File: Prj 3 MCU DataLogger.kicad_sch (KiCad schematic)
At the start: 25 parts, among them U1 24LC1025, U2 24LC1025, U3 DS1337S_, U4 ATMEGA328P-AU, Y1 16 MHz, Y2 32.768 KHz

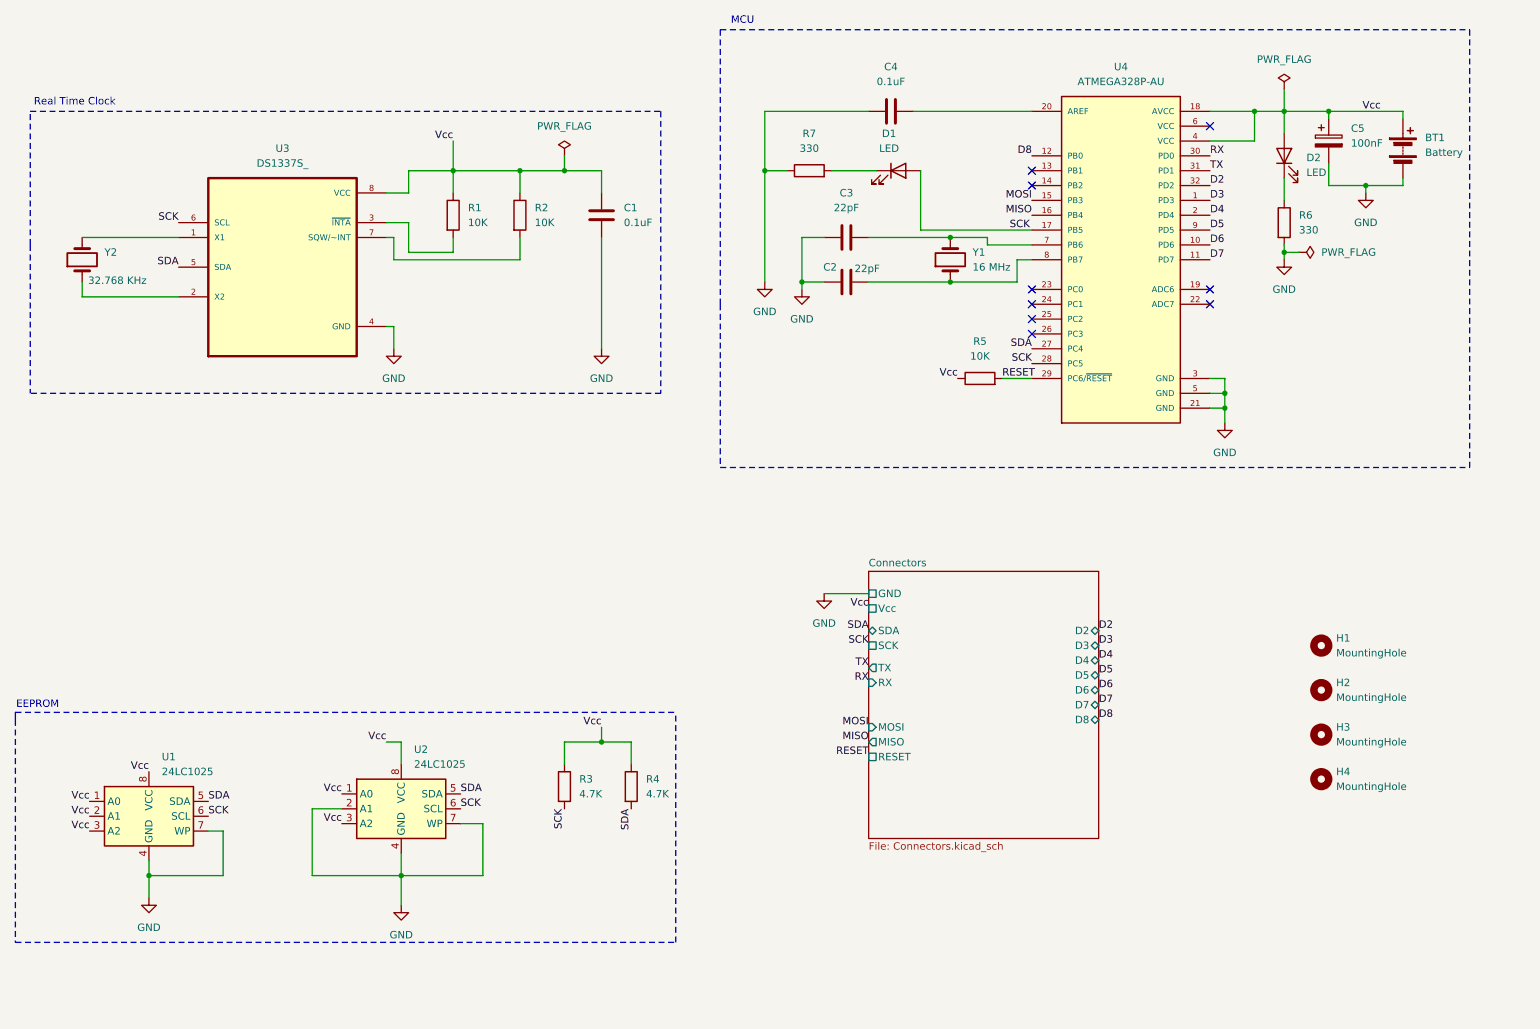
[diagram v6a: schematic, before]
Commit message: Fixed two defects in the schematic.
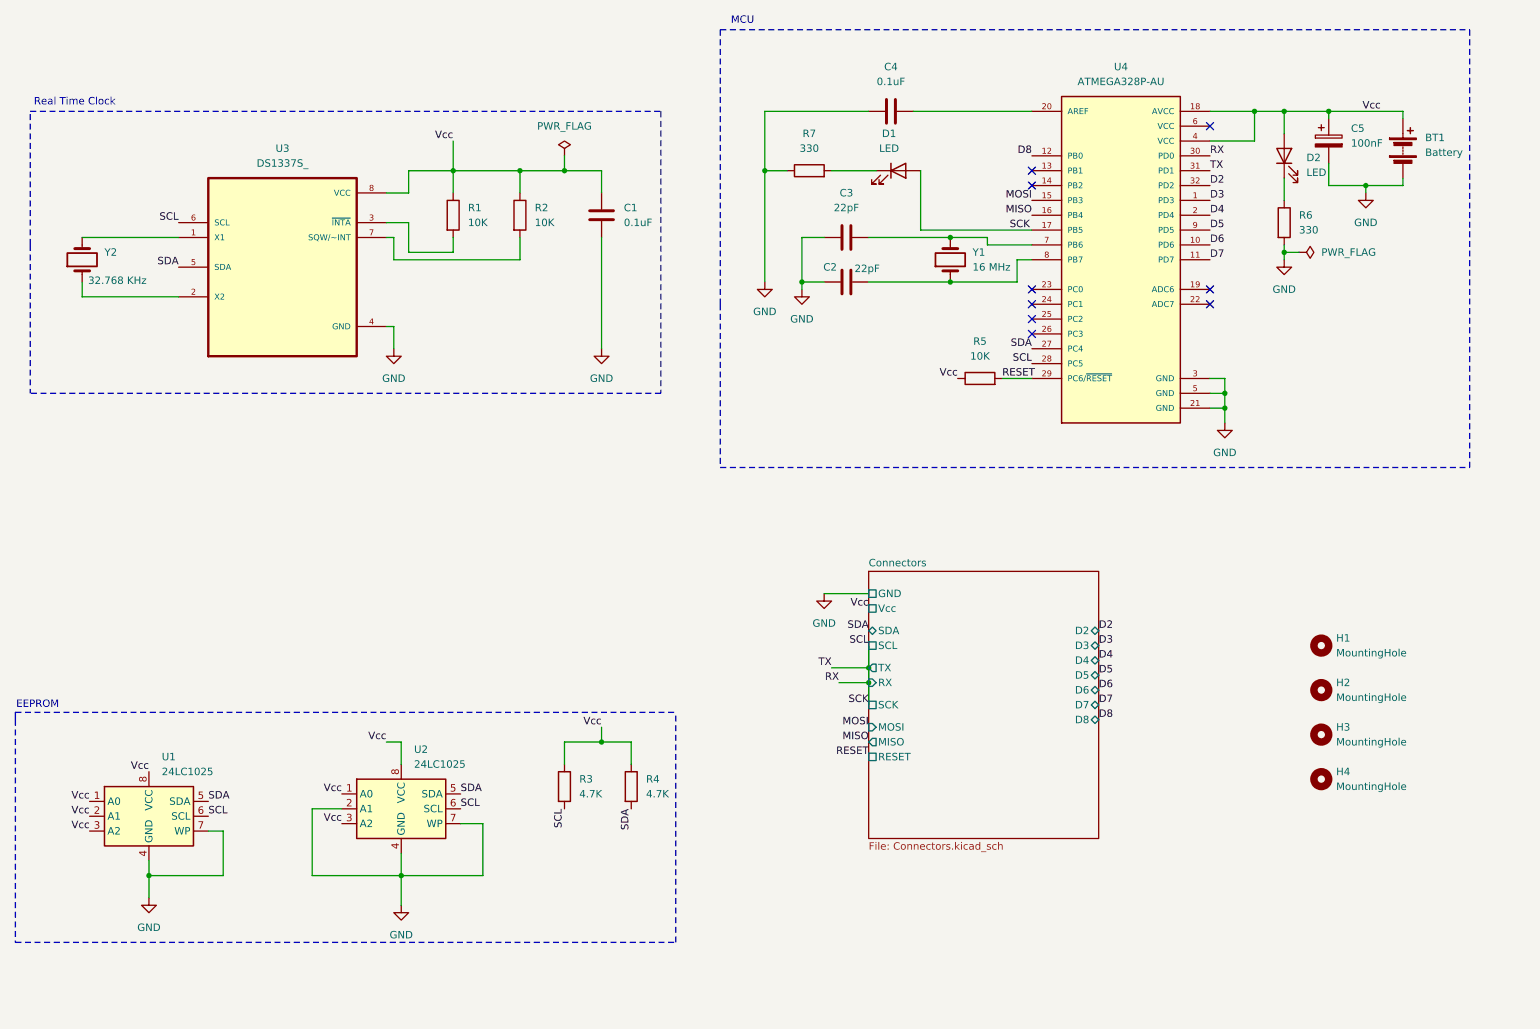
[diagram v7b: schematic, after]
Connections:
- net SCK is gone; now on net RX: D1.2 (A), R3.2, U1.6 (SCL), U2.6 (SCL), U3.6 (SCL), U4.17 (PB5), U4.28 (PC5)
- net TX is gone; now on net RX: U4.31 (PD1)
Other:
- sheet Connectors ports: added SCL; removed none
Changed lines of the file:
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@@
 	)
 	(junction
+		(at 171.45 129.54)
+		(diameter 0)
+		(color 0 0 0 0)
+	)
+	(junction
 		(at 256.54 46.99)
 		(diameter 0)
@@
 	)
 	(junction
+		(at 171.45 132.08)
+		(diameter 0)
+		(color 0 0 0 0)
+	)
+	(junction
 		(at 160.02 63.5)
 		(diameter 0)
@@
 	(wire
 		(pts
+			(xy 166.37 132.08) (xy 171.45 132.08)
+		)
+		(stroke
+			(width 0)
+			(type default)
+		)
+	)
+	(wire
+		(pts
 			(xy 229.87 34.29) (xy 237.49 34.29)
 		)
@@
 	(wire
 		(pts
+			(xy 171.45 132.08) (xy 171.45 129.54)
+		)
+		(stroke
+			(width 0)
+			(type default)
+		)
+	)
+	(wire
+		(pts
 			(xy 242.57 34.29) (xy 242.57 38.1)
 		)
@@
 	(wire
 		(pts
-			(xy 242.57 30.48) (xy 242.57 34.29)
+			(xy 171.45 135.89) (xy 171.45 132.08)
 		)
 		(stroke
@@
 	(wire
 		(pts
+			(xy 165.1 129.54) (xy 171.45 129.54)
+		)
+		(stroke
+			(width 0)
+			(type default)
+		)
+	)
+	(wire
+		(pts
+			(xy 171.45 129.54) (xy 171.45 125.73)
+		)
+		(stroke
+			(width 0)
+			(type default)
+		)
+	)
+	(wire
+		(pts
 			(xy 171.45 63.5) (xy 185.42 63.5)
 		)
@@
 		)
 	)
+	(label "SCL"
+		(at 58.42 154.94 0)
+		(fields_autoplaced yes)
+		(effects
+			(font
+				(size 1.27 1.27)
+			)
+			(justify left bottom)
+		)
+	)
 	(label "D2"
 		(at 229.87 46.99 0)
@@
 		)
 	)
-	(label "Vcc"
-		(at 81.28 151.13 180)
+	(label "SCL"
+		(at 101.6 153.67 0)
 		(fields_autoplaced yes)
 		(effects
@@
 				(size 1.27 1.27)
 			)
-			(justify right bottom)
+			(justify left bottom)
 		)
 	)
-	(label "SCK"
-		(at 119.38 153.67 270)
+	(label "Vcc"
+		(at 81.28 151.13 180)
 		(fields_autoplaced yes)
 		(effects
@@
 	)
 	(label "RX"
-		(at 171.45 132.08 180)
+		(at 166.37 132.08 180)
 		(fields_autoplaced yes)
 		(effects
@@
 		)
 	)
-	(label "SCK"
-		(at 171.45 125.73 180)
-		(fields_autoplaced yes)
-		(effects
-			(font
-				(size 1.27 1.27)
-			)
-			(justify right bottom)
-		)
-	)
 	(label "D5"
 		(at 229.87 54.61 0)
@@
 	)
 	(label "SCK"
-		(at 101.6 153.67 0)
+		(at 171.45 135.89 180)
 		(fields_autoplaced yes)
 		(effects
@@
 				(size 1.27 1.27)
 			)
-			(justify left bottom)
+			(justify right bottom)
 		)
 	)
@@
 		)
 	)
-	(label "SCK"
+	(label "SCL"
 		(at 199.39 77.47 180)
 		(fields_autoplaced yes)
@@
 		)
 	)
+	(label "SCL"
+		(at 53.34 53.34 180)
+		(fields_autoplaced yes)
+		(effects
+			(font
+				(size 1.27 1.27)
+			)
+			(justify right bottom)
+		)
+	)
 	(label "RESET"
 		(at 171.45 144.78 180)
@@
 	)
 	(label "TX"
-		(at 171.45 129.54 180)
+		(at 165.1 129.54 180)
 		(fields_autoplaced yes)
 		(effects
@@
 		)
 	)
+	(label "SCL"
+		(at 171.45 125.73 180)
+		(fields_autoplaced yes)
+		(effects
+			(font
+				(size 1.27 1.27)
+			)
+			(justify right bottom)
+		)
+	)
 	(label "D3"
 		(at 229.87 49.53 0)
@@
 		)
 	)
-	(label "SCK"
-		(at 53.34 53.34 180)
-		(fields_autoplaced yes)
-		(effects
-			(font
-				(size 1.27 1.27)
-			)
-			(justify right bottom)
-		)
-	)
 	(label "D4"
 		(at 229.87 52.07 0)
@@
 		)
 	)
-	(label "SCK"
-		(at 58.42 154.94 0)
+	(label "D7"
+		(at 229.87 59.69 0)
 		(fields_autoplaced yes)
 		(effects
@@
 		)
 	)
-	(label "D7"
-		(at 229.87 59.69 0)
+	(label "SCL"
+		(at 119.38 153.67 270)
 		(fields_autoplaced yes)
 		(effects
@@
 				(size 1.27 1.27)
 			)
-			(justify left bottom)
+			(justify right bottom)
 		)
 	)
@@
 	)
 	(symbol
-		(lib_id "power:PWR_FLAG")
-		(at 242.57 30.48 0)
-		(unit 1)
-		(exclude_from_sim no)
-		(in_bom yes)
-		(on_board yes)
-		(dnp no)
-		(fields_autoplaced yes)
-		(property "Reference" "#FLG01"
-			(at 242.57 28.575 0)
-			(effects
-				(font
-					(size 1.27 1.27)
-				)
-				(hide yes)
-			)
-		)
-		(property "Value" "PWR_FLAG"
-			(at 242.57 25.4 0)
-			(effects
-				(font
-					(size 1.27 1.27)
-				)
-			)
-		)
-		(property "Footprint" ""
-			(at 242.57 30.48 0)
-			(effects
-				(font
-					(size 1.27 1.27)
-				)
-				(hide yes)
-			)
-		)
-		(property "Datasheet" "~"
-			(at 242.57 30.48 0)
-			(effects
-				(font
-					(size 1.27 1.27)
-				)
-				(hide yes)
-			)
-		)
-		(property "Description" "Special symbol for telling ERC where power comes from"
-			(at 242.57 30.48 0)
-			(effects
-				(font
-					(size 1.27 1.27)
-				)
-				(hide yes)
-			)
-		)
-		(pin "1"
-		)
-		(instances
-			(project "Prj 3 MCU DataLogger"
-				(path "/bdc5bc67-61c4-474c-8492-5f30bea54457"
-					(reference "#FLG01")
-					(unit 1)
-				)
-			)
-		)
-	)
-	(symbol
 		(lib_id "Device:C")
 		(at 167.64 55.88 90)
@@
 		)
 		(pin "SCK" passive
-			(at 171.45 125.73 180)
+			(at 171.45 135.89 180)
 			(effects
 				(font
@@
 			(effects
 				(font
+					(size 1.27 1.27)
+				)
+				(justify left)
+			)
+		)
+		(pin "SCL" passive
+			(at 171.45 125.73 180)
+			(effects
+				(font
